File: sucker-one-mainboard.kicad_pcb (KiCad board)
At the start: 4 copper layers, 79.4 x 63 mm, 113 parts, among them J1 JST NC Valve, J10 JST Motor, J11 User Interface Module, J12 SWD, J2 JST NO Valve, J3 6P4C, J4 JST 3 Way Valve, Q1 BSS138, Q2 BSS138, Q3 BSS138, Q4 DMN15H310SE-13, SW1 Power Switch, SW2 Reset, U1 LD1117S33TR, U2 TPS61087DRCR, U3 STM32F103RBTx, U4 2SMPP-03, U5 INA125UA, Y1 8MHz(16pf)

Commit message: another wip
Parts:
- removed TP33: TP FOOTPEDAL AUX, TestPoint:TestPoint_Pad_D2.0mm
- added J5: AUX SPI, Connector_JST:JST_XH_B6B-XH-A_1x06_P2.50mm_Vertical, F.Cu at (94.5, 53.8)
- added J6: AUX I2C, Connector_JST:JST_XH_B4B-XH-A_1x04_P2.50mm_Vertical, F.Cu at (80.3, 53.8)
- Q4: footprint Package_TO_SOT_SMD:SOT-23 -> Package_TO_SOT_SMD:SOT-223
- TP1, TP10, TP11, TP12, TP13, TP14, TP15, TP16, TP17, TP18, TP19, TP2, TP22, TP23, TP24, TP25, TP26, TP27, TP28, TP29, TP3, TP30, TP31, TP32, TP4, TP5, TP6, TP7, TP8, TP9: moved to B.Cu
- moved TP30 111.5 mm to (76.7, 52.8)
- moved TP29 111.0 mm to (75.2, 55.9)
- moved TP19 103.3 mm to (83.3, 56.9)
- moved TP16 101.4 mm to (80.3, 56.9)
- moved TP17 100.1 mm to (69.6, 86.9)
- moved TP27 98.6 mm to (105.2, 56.9)
- moved TP24 98.5 mm to (88.4, 56.9)
- moved TP26 97.1 mm to (102.1, 56.9)
- moved TP23 96.1 mm to (91.4, 56.9)
- moved TP22 95.4 mm to (94.5, 56.9)
- moved TP28 92.1 mm to (108.2, 56.9)
- moved TP25 91.7 mm to (99.1, 56.9)
- moved TP31 86.4 mm to (80.8, 86.9)
- moved TP18 86.1 mm to (73.2, 86.9)
- moved TP32 80.0 mm to (98.0, 76.7)
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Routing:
- net Net-(F2-Pad1): track 0.00 -> 56.8 mm, vias 0 -> 3
- net USB_VIN: track 0.00 -> 56.6 mm, vias 0 -> 2
- net GND: track 0.00 -> 50.7 mm, vias 0 -> 12
- net +12V: track 0.00 -> 49.0 mm, vias 0 -> 1
- net VBUS: track 0.00 -> 47.2 mm, vias 0 -> 3
- net Net-(D1-Pad1): track 0.00 -> 27.9 mm, vias 0 -> 4
- net Net-(D1-Pad2): track 0.00 -> 27.6 mm, vias 0 -> 2
- net FOOTPEDAL_AUX: track 26.3 -> 0.00 mm
- net D+: track 0.00 -> 22.8 mm, vias 0 -> 1
- net D-: track 0.00 -> 22.1 mm, vias 0 -> 1
- net Net-(R2-Pad2): track 0.00 -> 19.8 mm
- net Net-(D11-Pad2): track 0.00 -> 18.6 mm
- net Net-(R7-Pad1): track 0.00 -> 15.8 mm, vias 0 -> 4
- net MOTOR_PWM: track 0.00 -> 12.8 mm, vias 0 -> 2
- net Net-(R1-Pad2): track 0.00 -> 10.3 mm
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
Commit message: routing finished
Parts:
- moved C22 22.6 mm to (84.6, 79.2), turned to 270 degrees
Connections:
- U2 pad 11: GNDA -> GND
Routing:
- net VBUS: track 47.2 -> 172.5 mm, vias 3 -> 10
- net +12V: track 49.0 -> 162.3 mm, vias 1 -> 4
- net NRST: track 0.00 -> 100.7 mm, vias 0 -> 4
- net SPI1_MOSI: track 0.00 -> 93.6 mm, vias 0 -> 9
- net I2C1_SCL: track 0.00 -> 89.8 mm, vias 0 -> 4
- net I2C1_SDA: track 0.00 -> 87.8 mm, vias 0 -> 2
- net FOOTPEDAL: track 0.72 -> 77.5 mm, vias 0 -> 4
- net VDDA: track 0.00 -> 64.6 mm, vias 0 -> 5
- net GND: track 50.7 -> 114.2 mm, vias 12 -> 41
- net SPI1_MISO: track 0.00 -> 56.4 mm, vias 0 -> 11
- net SPI1_CLK: track 0.00 -> 56.3 mm, vias 0 -> 7
- net NO_VALVE: track 0.00 -> 50.4 mm, vias 0 -> 2
- net D-: track 22.1 -> 71.0 mm, vias 1 -> 3
- net NC_VALVE: track 0.00 -> 45.8 mm, vias 0 -> 2
- net D+: track 22.8 -> 67.4 mm, vias 1 -> 3
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
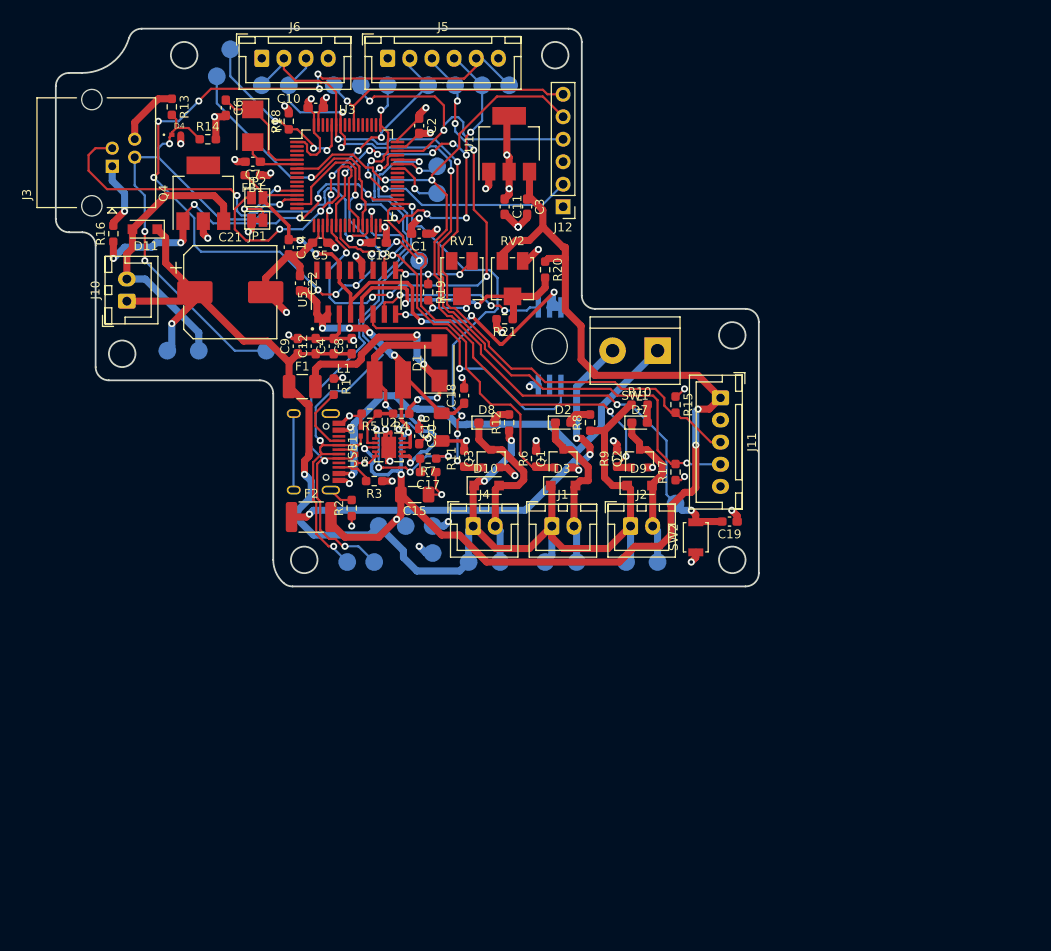
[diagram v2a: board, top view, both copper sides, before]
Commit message: added molex
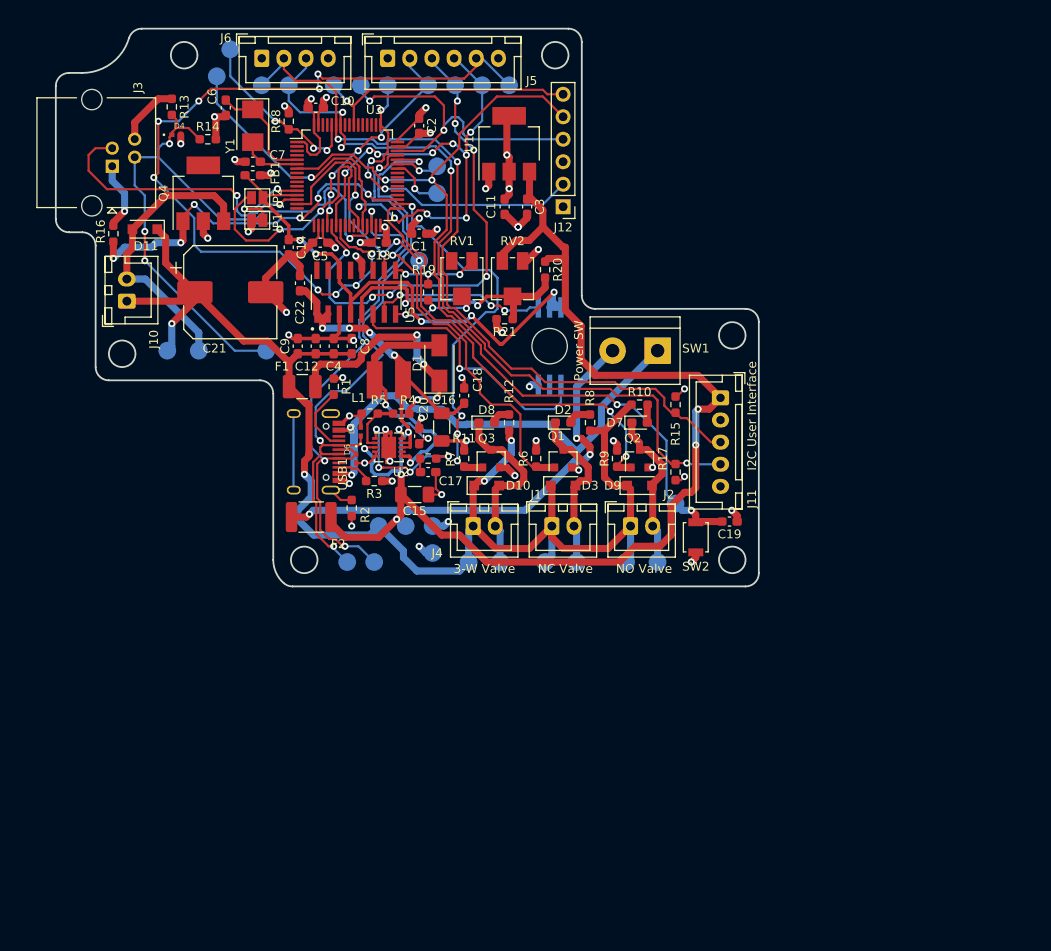
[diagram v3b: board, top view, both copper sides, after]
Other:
- board text added: "3-W Valve"
- board text added: "I2C User Interface"
- board text added: "NC Valve"
- board text added: "NO Valve"
- board text added: "Power SW"

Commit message: last changes and gerber files generated
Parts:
- removed J6: AUX I2C, Connector_JST:JST_XH_B4B-XH-A_1x04_P2.50mm_Vertical
- added D12: TPD1E05U06DPYR, TPD1E05U06DPYR:DIO_TPD1E05U06DPYR, F.Cu at (69.3, 66.5)
- J5: value AUX SPI -> EXP Port; footprint Connector_JST:JST_XH_B6B-XH-A_1x06_P2.50mm_Vertical -> 5034801000 (2):MOLEX_5034801000
- SW1: footprint TerminalBlock:TerminalBlock_bornier-2_P5.08mm -> Connector_JST:JST_XH_B2B-XH-A_1x02_P2.50mm_Vertical
- moved J5 5.48 mm to (99.8, 52.6)
- moved SW1 0.80 mm to (124.2, 86.6)
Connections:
- J5 pad 2: SPI1_CS -> VDD
- J5 pad 3: SPI1_CLK -> SPI1_CS
- J5 pad 4: SPI1_MISO -> SPI1_CLK
- J5 pad 5: SPI1_MOSI -> SPI1_MISO
- J5 pad 6: GND -> SPI1_MOSI
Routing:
- net I2C1_SCL: track 89.8 -> 105.7 mm, vias 4 -> 7
- net VDD: track 45.5 -> 56.3 mm, vias 11 -> 13
- net SPI1_MISO: track 56.4 -> 63.8 mm, vias 11 -> 12
- net I2C1_SDA: track 87.8 -> 94.5 mm, vias 2 -> 3
- net SPI1_MOSI: track 93.6 -> 99.0 mm
- net GND: track 114.2 -> 118.5 mm, vias 41 -> 45
- net SPI1_CLK: track 56.3 -> 58.7 mm, vias 7 -> 8
- net Net-(F2-Pad1): track 51.0 -> 53.2 mm
- net JTDO: track 30.1 -> 31.9 mm
- net USB_VIN: track 56.1 -> 57.8 mm
- net FOOTPEDAL_AUX: track 32.2 -> 33.8 mm
- net JTMS: track 36.4 -> 35.0 mm
- net SPI1_CS: track 25.2 -> 25.9 mm, vias 5 -> 6
- net JTCK: track 37.5 -> 37.0 mm
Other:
- board text added: "22.12.2020"
- board text added: "Expansion Port"
- board text added: "Mainboard v1.0"
- board text added: "Robin Reiter"
- board text added: "SPI & I2C"
- board text added: "Sucker One"
